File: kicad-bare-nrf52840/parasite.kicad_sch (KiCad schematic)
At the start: 53 parts, among them J1 TC2030-SWD, Q1 MMBT3906, Q4 Q_Photo_NPN, SW1 B3U-1000P, U1 nRF52840-QIAA, U2 SHTC3, Y1 32.768kHz, Y2 32MHz

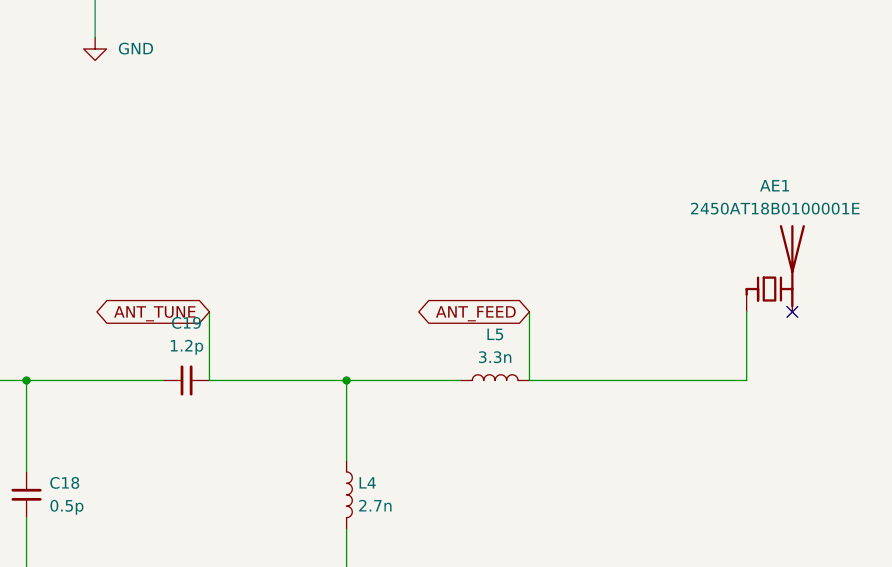
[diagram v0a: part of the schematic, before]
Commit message: feat: redesign for stocked antenna and capacitor with verified sensor ordering code
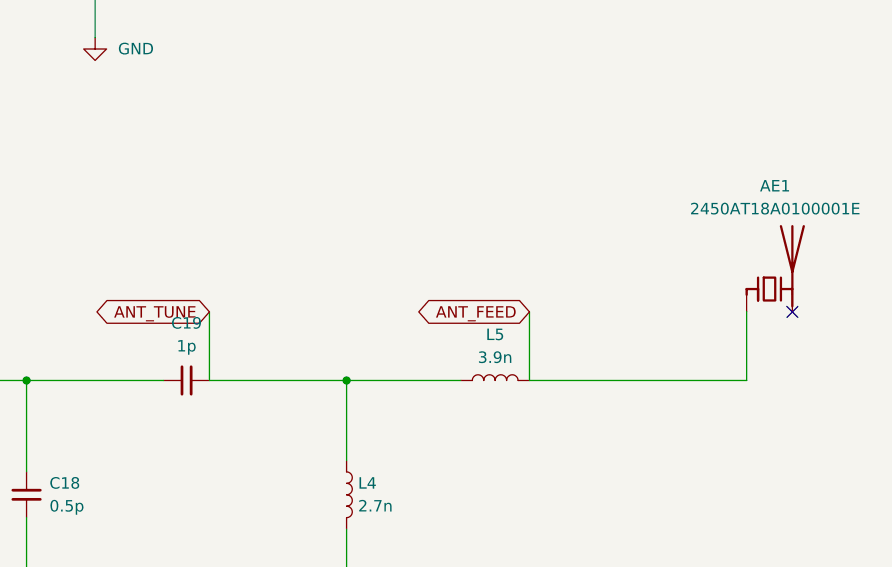
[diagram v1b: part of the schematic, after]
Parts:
- AE1: value 2450AT18B0100001E -> 2450AT18A0100001E; Assembly_note Tuning network starts at evaluation-board values; VNA tunin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 -> 2450AT18A antenna; 1.0pF / 2.7nH / 3.9nH prototype starting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; DigiKey (none) -> 712-2450AT18A0100001ECT-ND; LCSC C6055600 -> (none); MPN 2450AT18B0100001E -> 2450AT18A0100001E
- C1: DigiKey (none) -> 311-1036-1-ND; LCSC C1523 -> (none); MPN 0402B102K500NT -> CC0402KRX7R9BB102; Manufacturer FH -> YAGEO
- C10, C2, C5, C8, C9: DigiKey (none) -> 311-1338-1-ND; LCSC C1525 -> (none); MPN CL05B104KO5NNNC -> CC0402KRX7R7BB104; Manufacturer Samsung -> YAGEO
- C12: DigiKey (none) -> 311-1717-1-ND; LCSC C318631 -> (none); MPN CL05B473KA5NNNC -> CC0402KRX7R8BB473; Manufacturer Samsung -> YAGEO
- C13: DigiKey (none) -> 311-1024-1-ND; LCSC C26409 -> (none); MPN CL05C101JB5NNNC -> CC0402JRNPO9BN101; Manufacturer Samsung -> YAGEO
- C14, C15, C3, C4: DigiKey (none) -> 311-1016-1-ND; LCSC C1547 -> (none); MPN 0402CG120J500NT -> CC0402JRNPO9BN120; Manufacturer FH -> YAGEO
- C19: value 1.2p -> 1p; Assembly_note (none) -> Prototype antenna A matching value; tune with VNA.; DigiKey (none) -> 490-6206-1-ND; LCSC C76954 -> (none); MPN GRM1555C1H1R2BA01D -> GRM1555C1H1R0BA01D
- C6: footprint Capacitor_SMD:C_0402_1005Metric -> Capacitor_SMD:C_0603_1608Metric; Assembly_note (none) -> Larger 0603 bulk capacitor. Typical effective capacitance a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; Dielectric (none) -> X5R; DigiKey (none) -> 490-GRM188R61C475KE11JCT-ND; LCSC C23733 -> (none); MPN CL05A475MP5NRNC -> GRM188R61C475KE11J; Manufacturer Samsung -> Murata; Tolerance (none) -> 10%; Voltage (none) -> 16V
- D2: DigiKey (none) -> 160-1436-1-ND; LCSC C2286 -> (none); MPN KT-0603R -> LTST-C190KRKT; Manufacturer Hubei KENTO -> Lite-On
- L5: value 3.3n -> 3.9n; Assembly_note (none) -> Prototype antenna A matching value; tune with VNA.; DigiKey (none) -> 490-2617-1-ND; LCSC C86064 -> (none); MPN LQG15HS3N3S02D -> LQG15HS3N9S02D
- Q1: DigiKey (none) -> MMBT3906LT1GOSCT-ND; LCSC C2910191 -> (none); MPN MMBT3906 -> MMBT3906LT1G; Manufacturer JSCJ -> onsemi
- R1, R4, R7, R8: DigiKey (none) -> 311-10.0KLRCT-ND; LCSC C25744 -> (none); MPN 0402WGF1002TCE -> RC0402FR-0710KL; Manufacturer UNI-ROYAL -> YAGEO
- R10: DigiKey (none) -> 311-470LRCT-ND; LCSC C25117 -> (none); MPN 0402WGF4700TCE -> RC0402FR-07470RL; Manufacturer UNI-ROYAL -> YAGEO
- R2: DigiKey (none) -> 311-1.00KLRCT-ND; LCSC C11702 -> (none); MPN 0402WGF1001TCE -> RC0402FR-071KL; Manufacturer UNI-ROYAL -> YAGEO
- R6: DigiKey (none) -> 311-1.00MLRCT-ND; LCSC C26083 -> (none); MPN 0402WGF1004TCE -> RC0402FR-071ML; Manufacturer UNI-ROYAL -> YAGEO
- U2: DigiKey (none) -> 1649-SHTC3-TR-2.5KSCT-ND; MPN SHTC3 -> SHTC3-TR-2.5KS
- Y1: DigiKey (none) -> 644-STDMUA9-32.768KCT-ND; MPN NX3215SA-32.768K-STD-MUA-9 -> STDMUA9-32.768K

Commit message: feat: replace C18 with stocked RF capacitor and update complete assembly BOM
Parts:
- C18: Assembly_note (none) -> 0.5pF +/-0.05pF, 50V C0G high-Q RF capacitor, 0402; approve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; LCSC C88941 -> C76912; MPN GRM1555C1HR50WA01D -> GJM1555C1HR50WB01D; Source (none) -> JLCPCB C76912; Murata official specification verified
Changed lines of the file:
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@@
 			)
 		)
-		(property "Datasheet" ""
+		(property "Datasheet" "https://pim.murata.com/en-us/pim/details/?partNum=GJM1555C1HR50WB01%23"
 			(at 312.42 97.79 0)
 			(hide yes)
@@
 			)
 		)
-		(property "MPN" "GRM1555C1HR50WA01D"
+		(property "MPN" "GJM1555C1HR50WB01D"
 			(at 312.42 97.79 0)
 			(hide yes)
@@
 			)
 		)
-		(property "LCSC" "C88941"
+		(property "LCSC" "C76912"
 			(at 312.42 97.79 0)
 			(hide yes)
@@
 		(pin "2"
 		)
+		(property "Source" "JLCPCB C76912; Murata official specification verified"
+			(at 312.42 97.79 0)
+			(effects (font (size 1.27 1.27)) (hide yes))
+		)
+		(property "Assembly_note" "0.5pF +/-0.05pF, 50V C0G high-Q RF capacitor, 0402; approved replacement for GRM1555C1HR50WA01D"
+			(at 312.42 97.79 0)
+			(effects (font (size 1.27 1.27)) (hide yes))
+		)
 		(instances
